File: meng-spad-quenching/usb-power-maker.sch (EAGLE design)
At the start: 57 parts, among them IC1 LT1534-1, IC2 LT1534-1, IC22 TPS7A3001, IC24 TPS7A4901, IC25 TPS7A4901, X1 PN61729-S

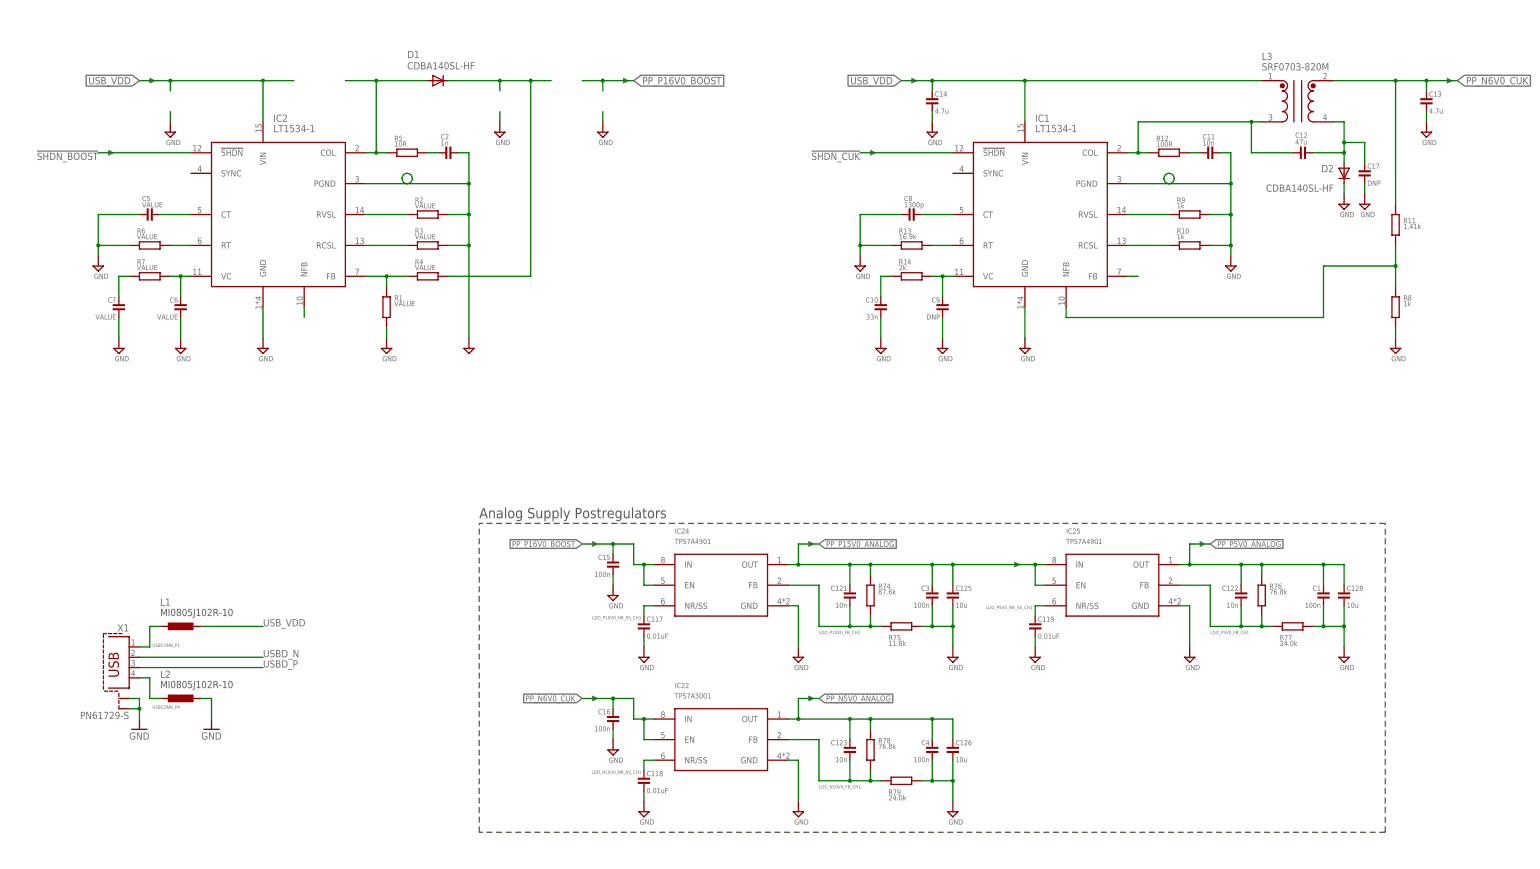
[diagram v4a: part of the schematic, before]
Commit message: Updated component values, added second-stage filters
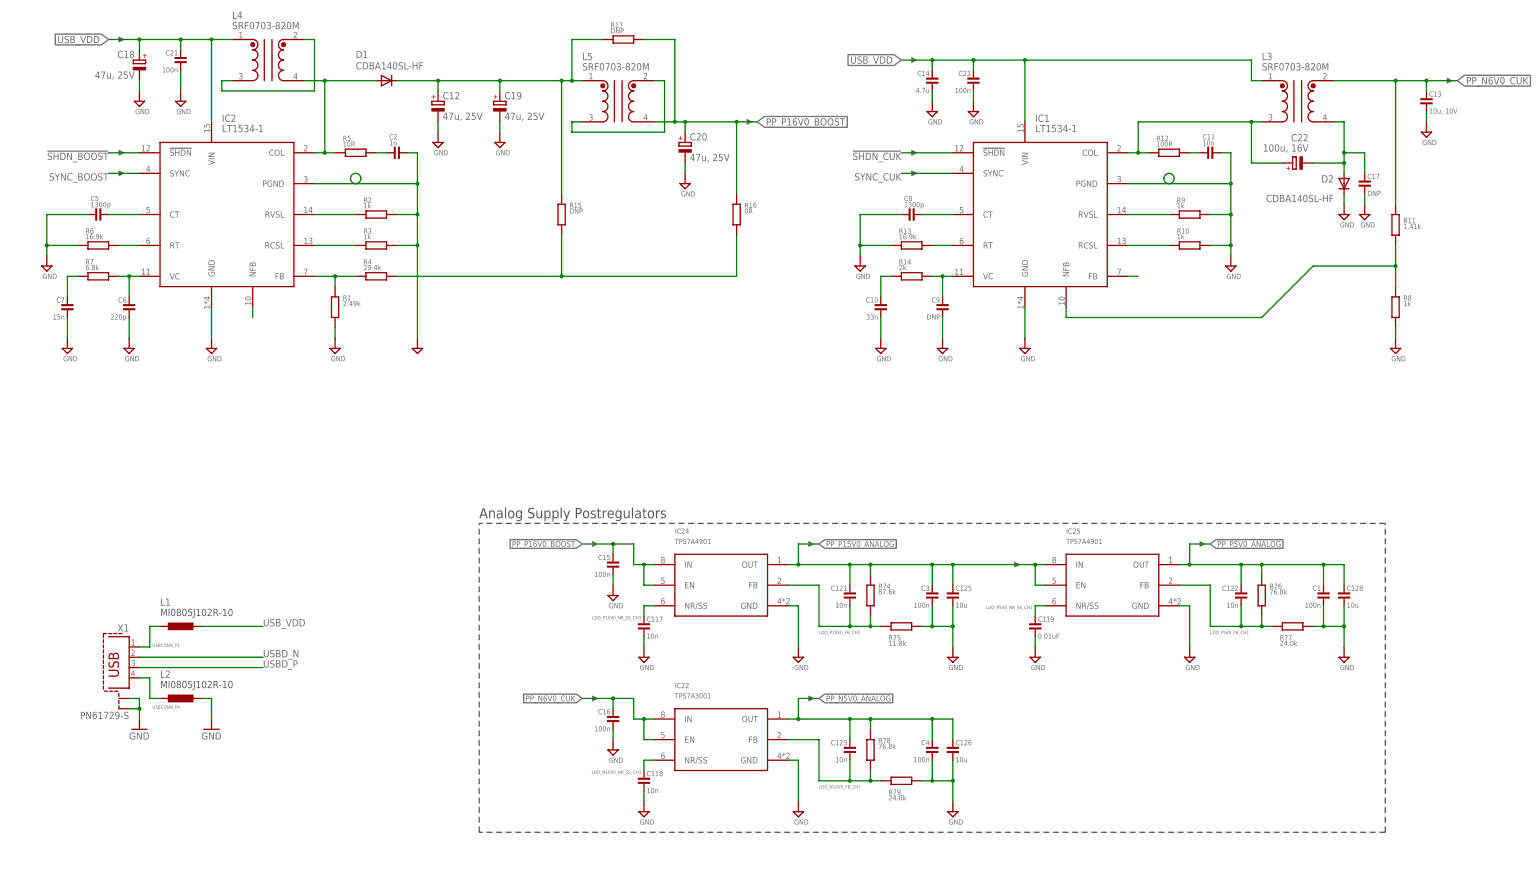
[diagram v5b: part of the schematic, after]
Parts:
- added C18, C19, C20: 47u, 25V, rcl:CPOL-EUE2.5-6
- added C21, C23: 100n, Bogdan_Commons:C0603
- added C22: 100u, 16V, rcl:CPOL-EUE2.5-6
- added L4, L5: SRF0703-820M, meng:SRF0703
- added R15, R17: DNP, GadgetFactory:R0603
- added R16: 0R, GadgetFactory:R0603
- C117, C118: value 0.01uF -> 10n
- C12: value 47u -> 47u, 25V; device Bogdan_Commons:C0805 -> rcl:CPOL-EUE2.5-6
- C13: value 4.7u -> 10u, 10V
- C5: value VALUE -> 1300p
- C6: value VALUE -> 220p
- C7: value VALUE -> 15n
- R1: value VALUE -> 2.49k
- R2, R3: value VALUE -> 1k
- R4: value VALUE -> 29.4k
- R6: value VALUE -> 16.9k
- R7: value VALUE -> 6.8k
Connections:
- removed net N$11: D1.C, R4A.1
- new net BOOST_STAGE1: C12.+, C19.+, D1.C, L5.1, R15A.2, R17A.2
- new net N$10: R15A.1, R16A.1, R4A.1
- new net N$3: L4.2, L4.3
- new net N$4: L5.2, L5.3
- new net SYNC_BOOST: IC2.SYNC
- new net SYNC_CUK: IC1.SYNC
- net GND: now also C12.-, C18.-, C19.-, C20.-, C21.2, C23.2
- net N$19: now also C22.-; no longer C12.2
- net N$28: now also C22.+; no longer C12.1
- net N$7: now also L4.4
- net PP_P16V0_BOOST: now also C20.+, L5.4, R16A.2, R17A.1
- net USB_VDD: now also C18.+, C21.1, C23.1, L4.1
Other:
- note added: "Bypass 2nd stage filter"
- note added: "Coupling Cap PN: RNU1C101MDS1JX"
- note added: "Select filter order"
- moved on the sheet: C14, C17, C2, C5, C6, C7, D1, D2, IC2, R1, R2, R3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
